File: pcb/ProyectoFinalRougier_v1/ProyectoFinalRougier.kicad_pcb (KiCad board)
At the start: 2 copper layers, 30 x 45 mm, 28 parts, among them J1 Screw_Terminal_01x02, J2 Screw_Terminal_01x02, J3 Conn_01x06, U1 AD8495, U2 AD8495, U3 TL431DBZ, U4 TL431DBZ

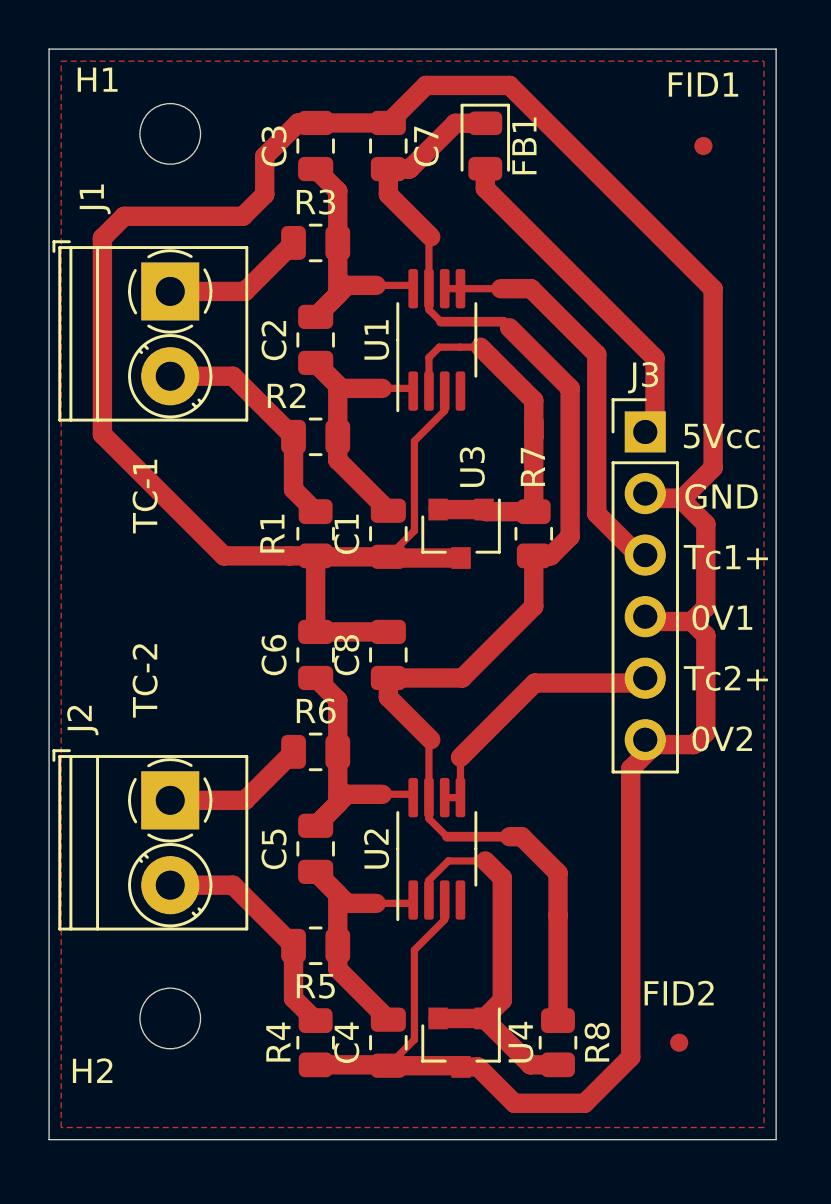
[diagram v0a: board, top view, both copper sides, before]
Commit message: Se agregan etiquetas y comentarios a los dos PCBs
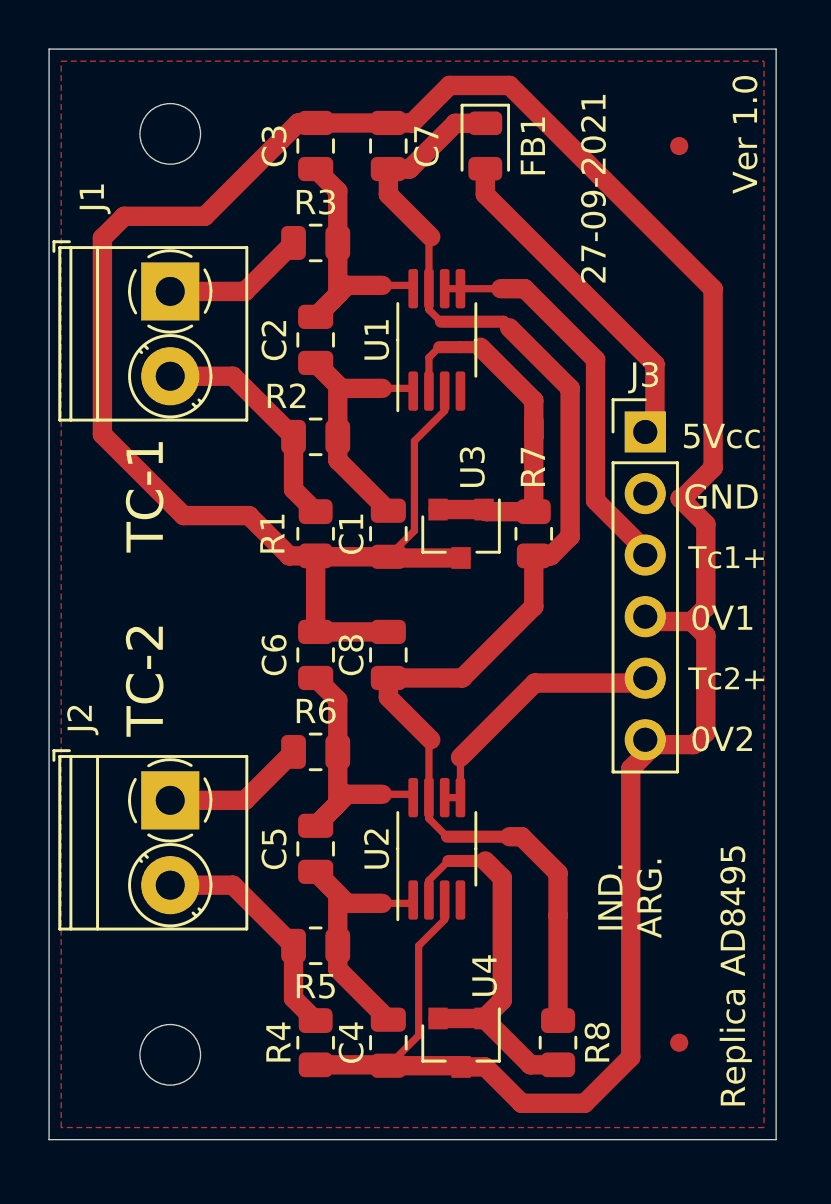
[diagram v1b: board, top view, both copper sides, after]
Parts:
- moved H2 1.50 mm to (125.0, 106.5)
- moved FID1 1.00 mm to (146.0, 69.0)
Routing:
- net GND: track 132.5 -> 129.5 mm
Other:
- net class Default: clearance 0.7 -> 0.8
- rule trace_clearance: 0.7 -> 0.8
- board text added: "27-09-2021"
- board text added: "GRILLAS BORDE PCB: Grilla 5.00 mm MARGEN: Grilla 0.5 mm POSICIONAMIENTO: Grila 1.00 mm RUTEO ANCHO DE PISTA GENERAL 0.80 mm - Grilla 1.00 mm ANCHO DE PISTA AD8495 0.25 mm - Grilla 0.25 mm MARGEN GENERAL 0.8 mm (Default) AD8495 0.2 mm FABRICANTE Se toma en cuenta la información de fabricación de Ernesto Mayer Carlos Pellegrini 1257/61 (B1604ASG) Florida Oeste Buenos Aires – Argentina - Tel.: +5411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"
- board text added: "IND. ARG."
- board text added: "NOTAS GENERALES"
- board text added: "Replica AD8495"
- board text added: "Terminación Superficial HASL (SnPb)"
- board text added: "Ver 1.0"

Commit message: Ajuste del Margen, se aumentó el menor margen que limita el AD8495
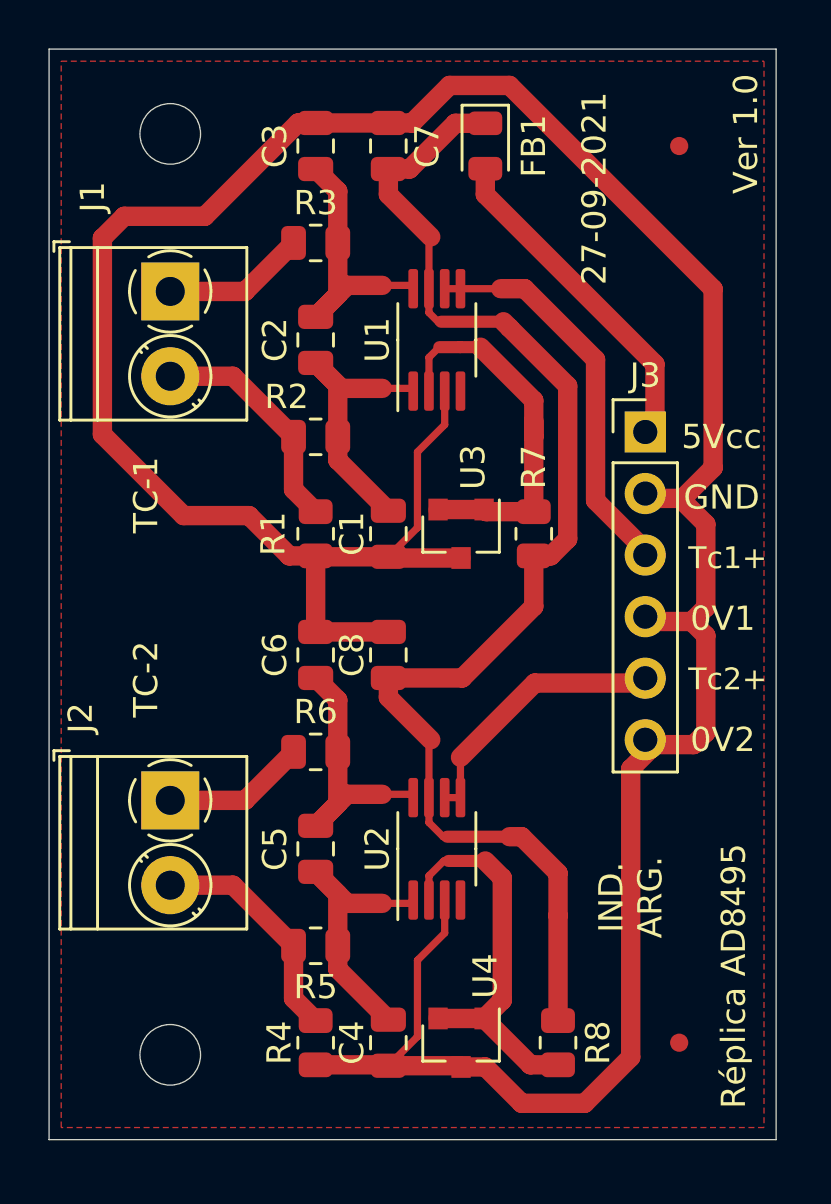
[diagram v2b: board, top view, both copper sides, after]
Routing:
- net GND: track 129.5 -> 131.1 mm
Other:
- net class AD8495: clearance 0.2 -> 0.28; trace_width 0.25 -> 0.3
- net class Default: trace_width 0.25 -> 0.3
- rule trace_min: 0.2 -> 0.3
- board text added: "GRILLAS BORDE PCB: Grilla 5.00 mm MARGEN: Grilla 0.5 mm POSICIONAMIENTO: Grila 1.00 mm RUTEO ANCHO DE PISTA GENERAL 0.80 mm - Grilla 1.00 mm ANCHO DE PISTA AD8495 0.30 mm - Grilla 0.20 mm MARGEN GENERAL 0.8 mm (Default) AD8495 0.30 mm FABRICANTE Se toma en cuenta la información de fabricación de Ernesto Mayer Carlos Pellegrini 1257/61 (B1604ASG) Florida Oeste Buenos Aires – Argentina - Tel.: +541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"
- board text added: "Réplica AD8495"
- board text removed: "GRILLAS BORDE PCB: Grilla 5.00 mm MARGEN: Grilla 0.5 mm POSICIONAMIENTO: Grila 1.00 mm RUTEO ANCHO DE PISTA GENERAL 0.80 mm - Grilla 1.00 mm ANCHO DE PISTA AD8495 0.25 mm - Grilla 0.25 mm MARGEN GENERAL 0.8 mm (Default) AD8495 0.2 mm FABRICANTE Se toma en cuenta la información de fabricación de Ernesto Mayer Carlos Pellegrini 1257/61 (B1604ASG) Florida Oeste Buenos Aires – Argentina - Tel.: +5411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"
- board text removed: "Replica AD8495"
